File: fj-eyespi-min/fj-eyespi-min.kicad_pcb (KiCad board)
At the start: 2 copper layers, 45.6 x 24.7 mm, 2 parts, among them J1 Conn_01x18_Socket, J2 Conn_02x16_Odd_Even

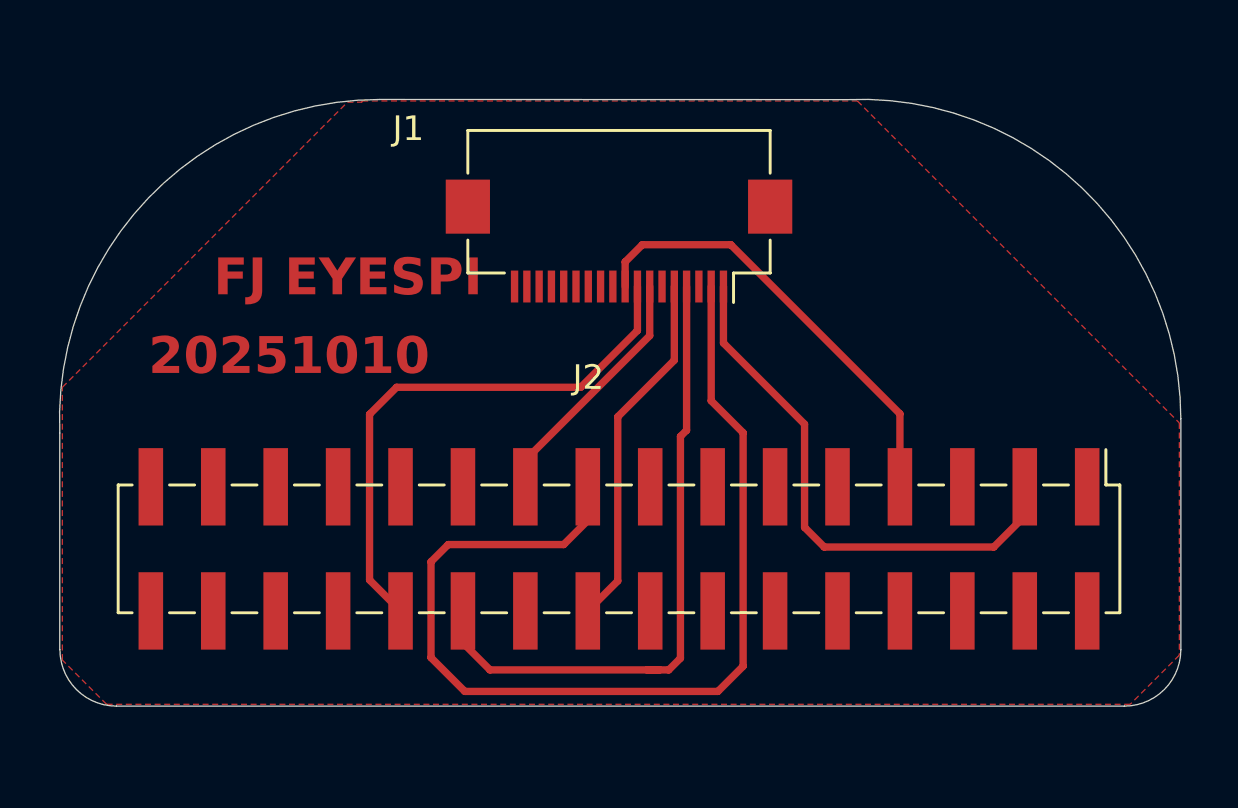
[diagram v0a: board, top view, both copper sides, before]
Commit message: silkscreen re-orient
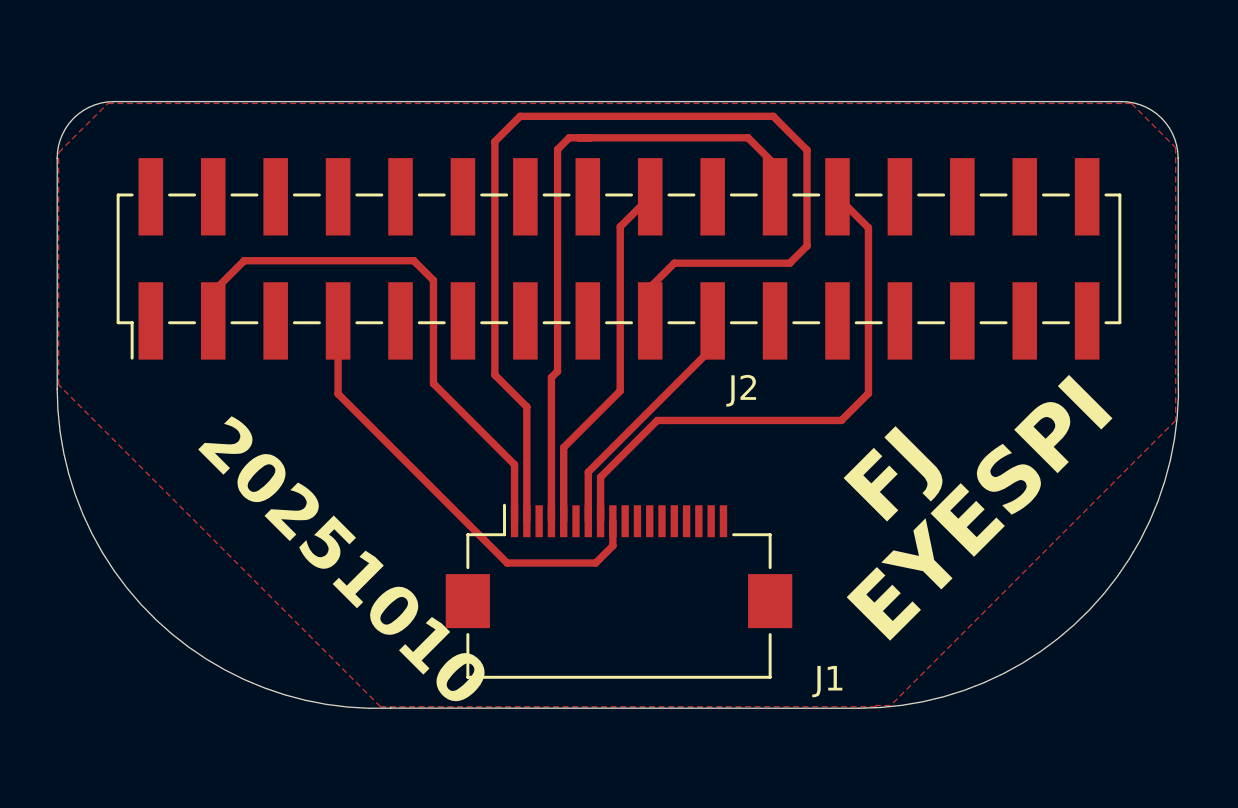
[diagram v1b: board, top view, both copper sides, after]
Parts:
- moved J1 13.2 mm to (155.9, 94.7), turned to 0 degrees
- moved J2 11.8 mm to (155.9, 82.2), turned to 90 degrees
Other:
- outline, holes or cut-outs redrawn
- board text added: "EYESPI"
- board text added: "FJ"
- board text removed: "FJ EYESPI"

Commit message: updated connector orientation
Flipped pin 1 and pin 18 direction by moving tracks for FFC connector
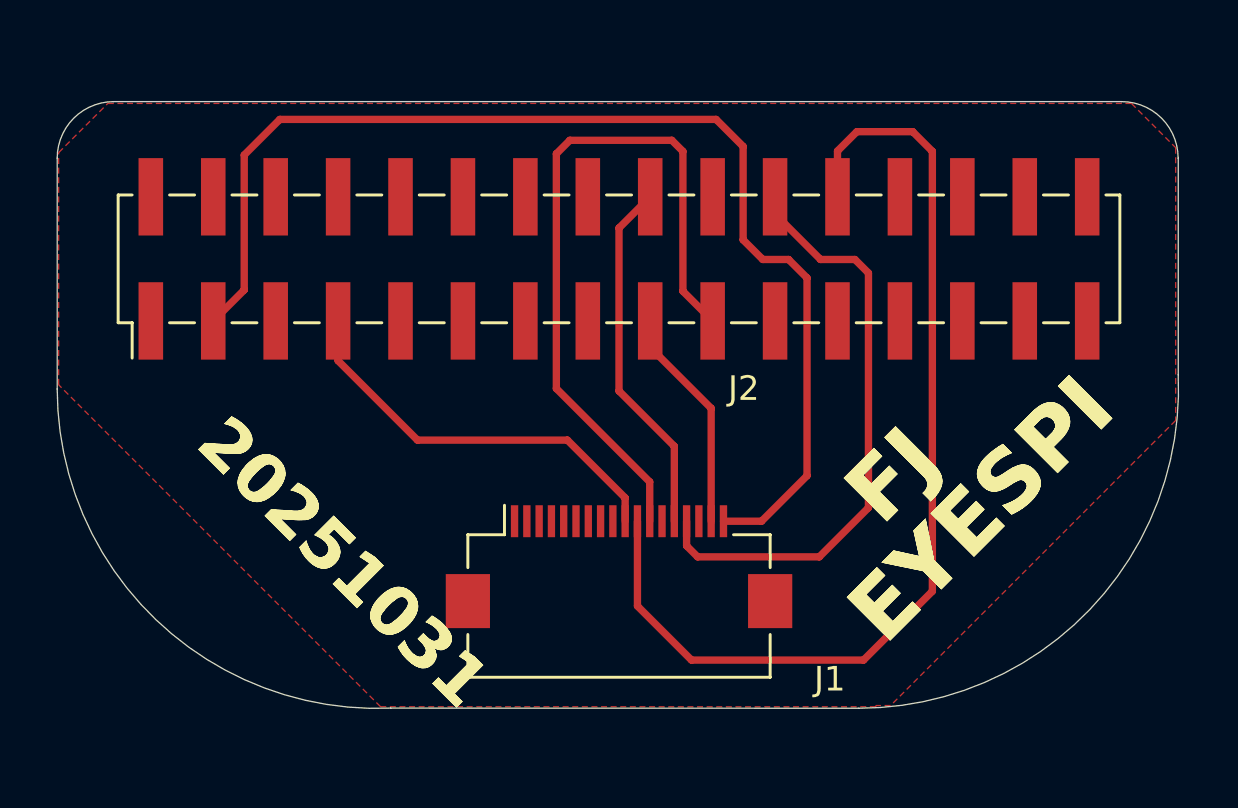
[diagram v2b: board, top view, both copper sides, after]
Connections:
- J1 pad 1: 3v3 -> unconnected-(J1-Pin_1-Pad1)
- J1 pad 10: unconnected-(J1-Pin_10-Pad10) -> /disp_cs
- J1 pad 11: unconnected-(J1-Pin_11-Pad11) -> /reset
- J1 pad 12: unconnected-(J1-Pin_12-Pad12) -> /dc
- J1 pad 14: unconnected-(J1-Pin_14-Pad14) -> /mosi
- J1 pad 15: unconnected-(J1-Pin_15-Pad15) -> /sck
- J1 pad 16: unconnected-(J1-Pin_16-Pad16) -> gnd
- J1 pad 17: unconnected-(J1-Pin_17-Pad17) -> /backlite
- J1 pad 18: unconnected-(J1-Pin_18-Pad18) -> 3v3
- J1 pad 2: /backlite -> unconnected-(J1-Pin_2-Pad2)
- J1 pad 3: gnd -> unconnected-(J1-Pin_3-Pad3)
- J1 pad 4: /sck -> unconnected-(J1-Pin_4-Pad4)
- J1 pad 5: /mosi -> unconnected-(J1-Pin_5-Pad5)
- J1 pad 7: /dc -> unconnected-(J1-Pin_7-Pad7)
- J1 pad 8: /reset -> unconnected-(J1-Pin_8-Pad8)
- J1 pad 9: /disp_cs -> unconnected-(J1-Pin_9-Pad9)
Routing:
- net /backlite: track 42.0 -> 9.18 mm
- net 3v3: track 22.2 -> 47.9 mm
- net /dc: track 10.2 -> 29.5 mm
- net /reset: track 22.6 -> 41.8 mm
- net /sck: track 26.5 -> 24.5 mm
- net /disp_cs: track 18.3 -> 16.6 mm
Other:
- board text added: "20251031"
- board text removed: "20251010"

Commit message: working display
jumper wired with ada breakout

| Signal         | Pin Name | Function / Purpose   |
| -------------- | -------- | -------------------- |
| SCK            | SCK      | SPI Clock            |
| MOSI           | MOSI     | SPI Data (Host→LCD)  |
| MISO           | —        | Not used             |
| CS             | D9       | Chip Select (TCS)    |
| DC             | D7       | Data/Command         |
| RST            | D8       | Reset                |
| Backlight (BL) | D6       | LED Backlight Enable |
| VCC            | 3V / 5V  | Power Supply         |
| GND            | GND      | Ground               |
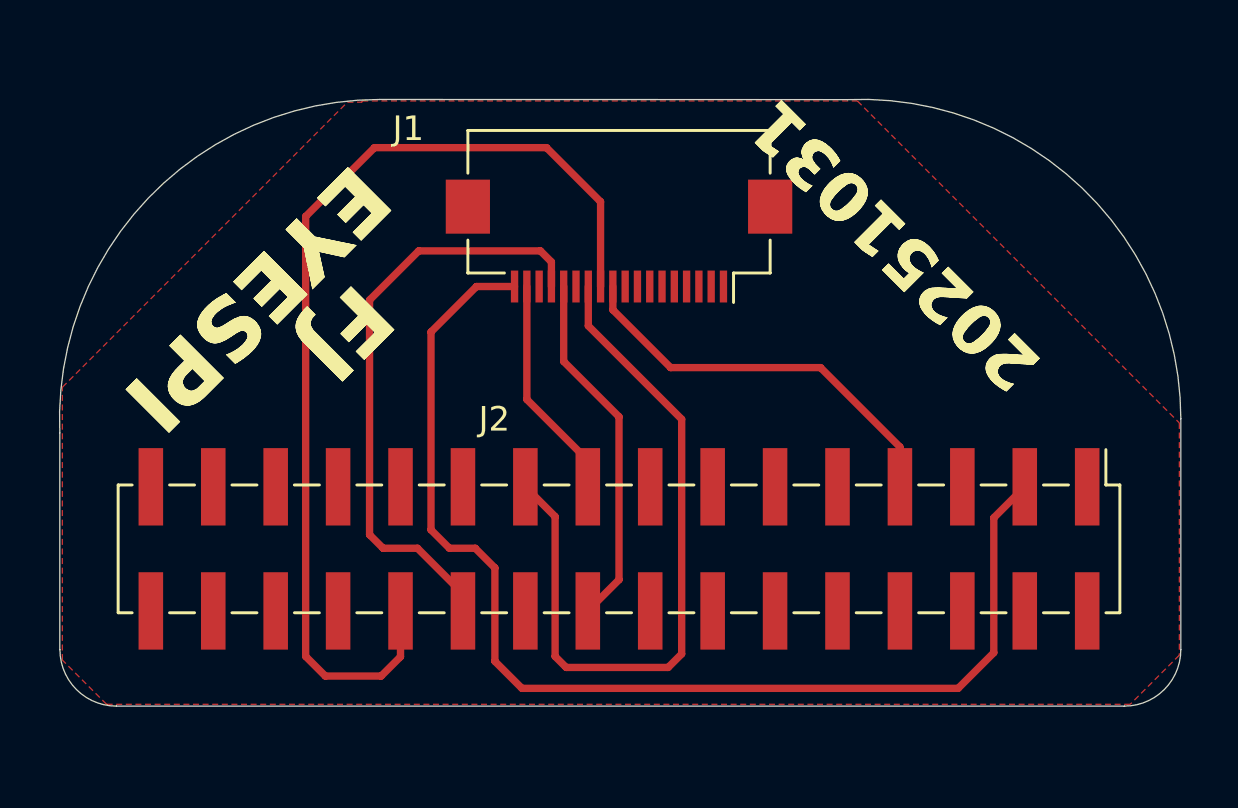
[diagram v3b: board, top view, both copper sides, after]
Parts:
- moved J1 13.2 mm to (155.9, 81.5), turned to 180 degrees
- moved J2 11.8 mm to (155.9, 94.0), turned to -90 degrees
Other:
- outline, holes or cut-outs redrawn
